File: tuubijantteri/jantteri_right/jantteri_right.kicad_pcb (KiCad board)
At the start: 2 copper layers, 129.3 x 64.5 mm, 83 parts, among them J1 USB_C_Receptacle_USB2.0, J2 Conn_01x02_Male, J3 Conn_01x02_Male, J4 Conn_02x08_Odd_Even, Q1 AP3407, Q2 AP3404S, Q3 AP3404S, Q4 AP3404S, Q5 AP3407, U1 STUSB4500QTR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

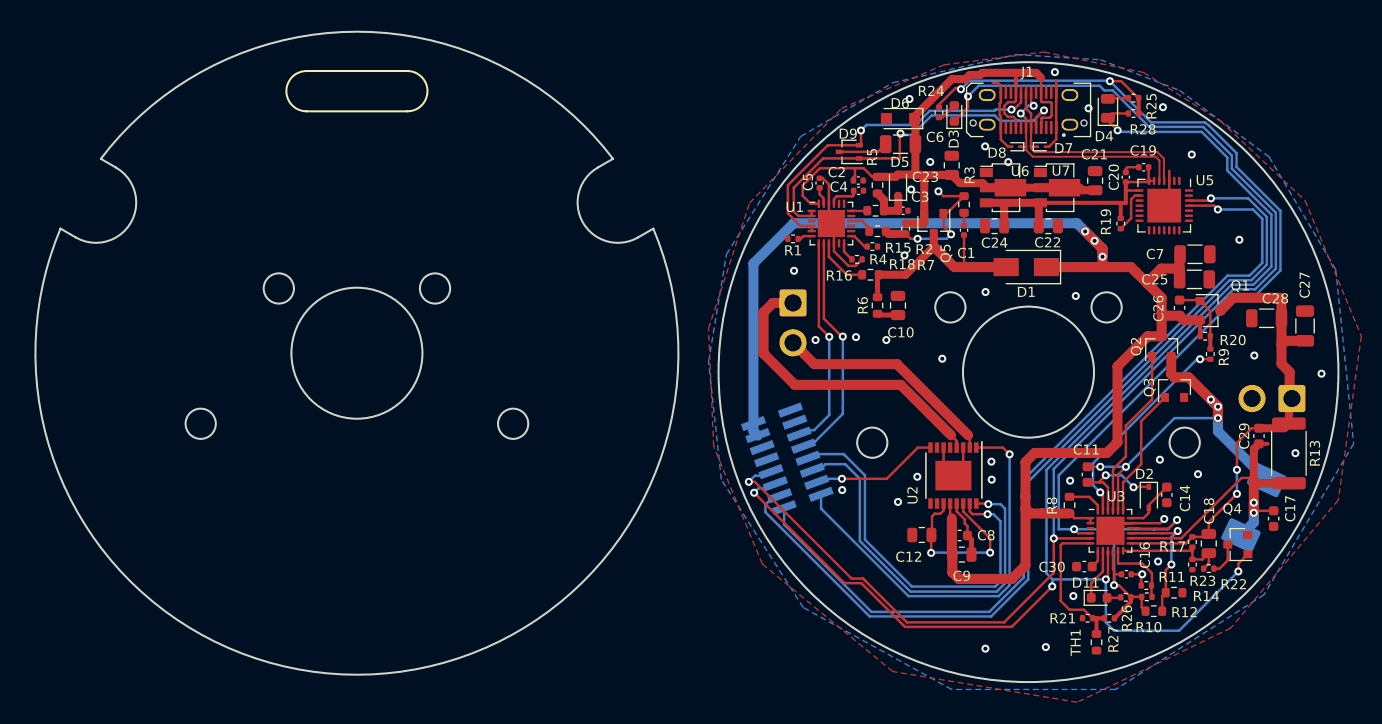
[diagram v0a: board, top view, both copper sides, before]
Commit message: Update jantteri-right to new layout
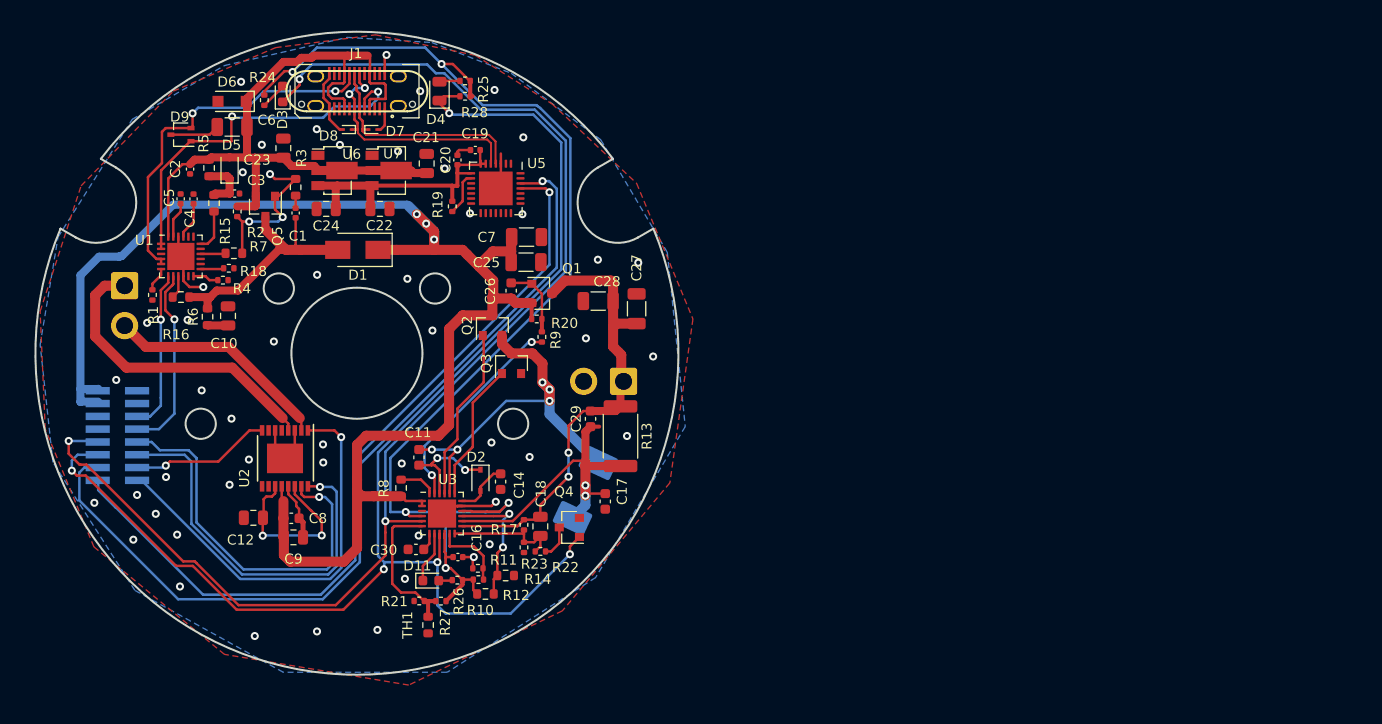
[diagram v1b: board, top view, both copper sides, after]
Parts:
- moved R16 68.4 mm to (121.6, 79.7)
- moved R24 66.9 mm to (129.9, 60.2)
- moved D3 66.7 mm to (131.7, 59.5)
- moved J1 66.7 mm to (139.1, 59.3)
- moved J4 66.5 mm to (115.3, 93.4), turned to 180 degrees
- moved R6 66.5 mm to (124.3, 81.6)
- moved C10 66.5 mm to (126.3, 81.6)
- moved Q2 66.4 mm to (152.5, 82.5)
- moved C3 66.3 mm to (127.0, 69.4)
- moved J3 66.3 mm to (116.1, 78.6)
- moved C1 66.3 mm to (133.0, 71.3)
- moved C11 66.3 mm to (145.3, 95.6)
- moved C12 66.3 mm to (128.8, 101.6)
- moved C16 66.3 mm to (149.1, 105.5)
- moved C17 66.3 mm to (163.7, 100.0)
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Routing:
- net GND: track 55.5 -> 47.0 mm, vias 35 -> 50
- net SCL_out: track 21.2 -> 16.0 mm
- net RXD_out: track 84.9 -> 79.9 mm
- net SDA_out: track 23.1 -> 18.8 mm
- net /Sheet65F09169/VSINK: track 21.8 -> 25.6 mm
- net Net-(R16-Pad1): track 5.38 -> 2.30 mm
- net TXD_out: track 90.0 -> 87.4 mm
- net Net-(R15-Pad1): track 1.60 -> 4.15 mm
- net /Sheet65F09169/CC2: track 34.5 -> 36.9 mm
- net /Sheet65F0AC28/VREF: track 125.2 -> 123.1 mm
- net Net-(C5-Pad2): track 1.76 -> 3.58 mm
- net STAT2_out: track 141.2 -> 139.4 mm
- net V_SYSTEM_out: track 144.6 -> 145.9 mm
- net STAT1_out: track 130.7 -> 129.5 mm
- net DRV_n_FAULT_out: track 13.0 -> 14.2 mm
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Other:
- board size 129.3 x 64.5 mm -> 63.8 x 63.8 mm
- board text added: "B+"
- board text added: "B-"
- board text added: "GND"
- board text added: "M+"
- board text added: "M-"
- board text added: "VOUT"

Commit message: update jantteri_right
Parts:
- moved L1 0.55 mm to (161.8, 98.3), turned to 270 degrees
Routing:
- net Net-(C17-Pad2): track 32.0 -> 31.3 mm

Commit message: Update projects
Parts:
- removed D1: SS34, Diode_SMD:D_SMA
- added C13: 0u1, Capacitor_SMD:C_0603_1608Metric, F.Cu at (140.8, 76.8)
- added C15: 1u, Capacitor_SMD:C_0603_1608Metric, F.Cu at (142.0, 97.7)
- added C31: 0u1, Capacitor_SMD:C_0603_1608Metric, F.Cu at (139.2, 100.2)
- added Q6: AP3407, Package_TO_SOT_SMD:SOT-23, F.Cu at (136.8, 74.1)
- added Q7: AP3407, Package_TO_SOT_SMD:SOT-23, F.Cu at (140.8, 74.1)
- added R29: 100K, Resistor_SMD:R_0402_1005Metric, F.Cu at (136.4, 76.8)
- added R30: 1K, Resistor_SMD:R_0402_1005Metric, F.Cu at (147.6, 85.5)
- R17: value 560K -> 160K
- R22: value 1M -> 200K
- R23: value 100K -> 30K
- R24, R26: value 10K -> 100R
- R25: value 10K -> 33R
- moved Q2 14.5 mm to (144.6, 94.7), turned to 180 degrees
- moved Q3 10.2 mm to (148.6, 94.6), turned to 180 degrees
- moved C7 3.77 mm to (152.4, 75.1), turned to -90 degrees
- moved Q1 3.72 mm to (158.0, 75.6)
- moved R8 3.37 mm to (141.2, 96.2), turned to 0 degrees
- moved R9 2.45 mm to (156.0, 81.7)
- moved R20 2.26 mm to (155.5, 80.1)
- moved C11 2.00 mm to (146.1, 97.4), turned to 0 degrees
- moved C1 1.72 mm to (133.0, 73.1)
- moved C25 1.43 mm to (155.0, 75.1), turned to -90 degrees
- moved C26 1.38 mm to (155.7, 78.6), turned to 180 degrees
- moved D4 0.71 mm to (146.6, 59.3)
- moved D2 0.58 mm to (151.4, 98.4)
- moved C14 0.21 mm to (153.4, 98.2), turned to -90 degrees
- moved D3 0.11 mm to (131.9, 59.5)
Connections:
- net /Sheet66043151/3V3_out renamed /Sheet6602CEA0/VIO
- J1 pad A8: Net-(J1-PadA8) -> unconnected-(J1-SBU1-PadA8)
- J1 pad B8: Net-(J1-PadB8) -> unconnected-(J1-SBU2-PadB8)
- J1 pad S1: Net-(J1-PadS1) -> unconnected-(J1-SHIELD-PadS1)_2
- J4 pad 14: TXD_out -> RXD_out
- J4 pad 16: RXD_out -> TXD_out
- J4 pad 6: Net-(J4-Pad6) -> unconnected-(J4-Pin_6-Pad6)
- J4 pad 8: Net-(J4-Pad8) -> unconnected-(J4-Pin_8-Pad8)
- R8 pad 1: V_SYSTEM_out -> Net-(Q6-S)
- U1 pad 11: Net-(U1-Pad11) -> unconnected-(U1-ATTACH-Pad11)
- U1 pad 14: Net-(U1-Pad14) -> unconnected-(U1-POWER_OK3-Pad14)
- U1 pad 15: Net-(U1-Pad15) -> unconnected-(U1-GPIO-Pad15)
- U1 pad 17: Net-(U1-Pad17) -> unconnected-(U1-A_B_SIDE-Pad17)
- U1 pad 19: Net-(U1-Pad19) -> unconnected-(U1-ALERT-Pad19)
- U1 pad 20: Net-(U1-Pad20) -> unconnected-(U1-POWER_OK2-Pad20)
- U1 pad 3: Net-(U1-Pad3) -> unconnected-(U1-NC-Pad3)
- U2 pad 10: Net-(U2-Pad10) -> unconnected-(U2-BIN2-Pad10)
- U2 pad 5: Net-(U2-Pad5) -> unconnected-(U2-BOUT2-Pad5)
- U2 pad 7: Net-(U2-Pad7) -> unconnected-(U2-BOUT1-Pad7)
- U2 pad 9: Net-(U2-Pad9) -> unconnected-(U2-BIN1-Pad9)
- U5 pad 1: Net-(U5-Pad1) -> unconnected-(U5-~{DCD}-Pad1)
- U5 pad 10: Net-(U5-Pad10) -> unconnected-(U5-NC-Pad10)
- U5 pad 11: Net-(U5-Pad11) -> unconnected-(U5-~{SUSPENDb}-Pad11)
- U5 pad 12: Net-(U5-Pad12) -> unconnected-(U5-SUSPEND-Pad12)
- U5 pad 13: Net-(U5-Pad13) -> unconnected-(U5-CHREN-Pad13)
- U5 pad 14: Net-(U5-Pad14) -> unconnected-(U5-CHR1-Pad14)
- U5 pad 15: Net-(U5-Pad15) -> unconnected-(U5-CHR0-Pad15)
- U5 pad 16: Net-(U5-Pad16) -> unconnected-(U5-~{WAKEUP}/GPIO.3-Pad16)
- U5 pad 17: Net-(U5-Pad17) -> unconnected-(U5-RS485/GPIO.2-Pad17)
- U5 pad 18: Net-(U5-Pad18) -> unconnected-(U5-~{RXT}/GPIO.1-Pad18)
- U5 pad 19: Net-(U5-Pad19) -> unconnected-(U5-~{TXT}/GPIO.0-Pad19)
- U5 pad 2: Net-(U5-Pad2) -> unconnected-(U5-~{RI}/CLK-Pad2)
- U5 pad 20: Net-(U5-Pad20) -> unconnected-(U5-GPIO.6-Pad20)
- U5 pad 21: Net-(U5-Pad21) -> unconnected-(U5-GPIO.5-Pad21)
- U5 pad 22: Net-(U5-Pad22) -> unconnected-(U5-GPIO.4-Pad22)
- U5 pad 23: Net-(U5-Pad23) -> unconnected-(U5-~{CTS}-Pad23)
- U5 pad 24: Net-(U5-Pad24) -> unconnected-(U5-~{RTS}-Pad24)
- U5 pad 27: Net-(U5-Pad27) -> unconnected-(U5-~{DSR}-Pad27)
- U5 pad 28: Net-(U5-Pad28) -> unconnected-(U5-~{DTR}-Pad28)
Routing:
- net Net-(Q6-S): track 0.00 -> 45.3 mm, vias 0 -> 6
- net Net-(U3-ACDRV): track 0.00 -> 29.0 mm, vias 0 -> 2
- net Net-(Q6-G): track 0.00 -> 20.9 mm
- net Net-(Q2-G): track 17.3 -> 5.62 mm
- net Net-(Q3-G): track 13.8 -> 3.94 mm
- net V_SYSTEM_out: track 145.9 -> 138.6 mm
- net TXD_out: track 87.4 -> 81.6 mm
- net /Sheet65F09169/VSINK: track 25.6 -> 22.4 mm
- net Net-(Q5-G): track 15.9 -> 12.8 mm, vias 3 -> 0
- net Net-(U3-BATDRV): track 21.0 -> 24.1 mm
- net Net-(Q2-S): track 39.4 -> 36.5 mm, vias 5 -> 3
- net Net-(U3-VCC): track 3.70 -> 6.06 mm
- net GND: track 47.0 -> 49.0 mm, vias 50 -> 54
- net Net-(C1-Pad2): track 1.25 -> 2.97 mm
- net DRV_SLEEP_out: track 41.4 -> 39.9 mm
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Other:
- net class Default removed
